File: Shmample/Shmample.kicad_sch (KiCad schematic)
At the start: 148 parts, among them J1 Conn_01x04_Socket, J2 PowerOut, Q1 BC547, Q10 BC547, Q2 BC557, Q3 BC547, Q4 BC547, Q5 BC557, Q6 BC557, Q7 BC547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

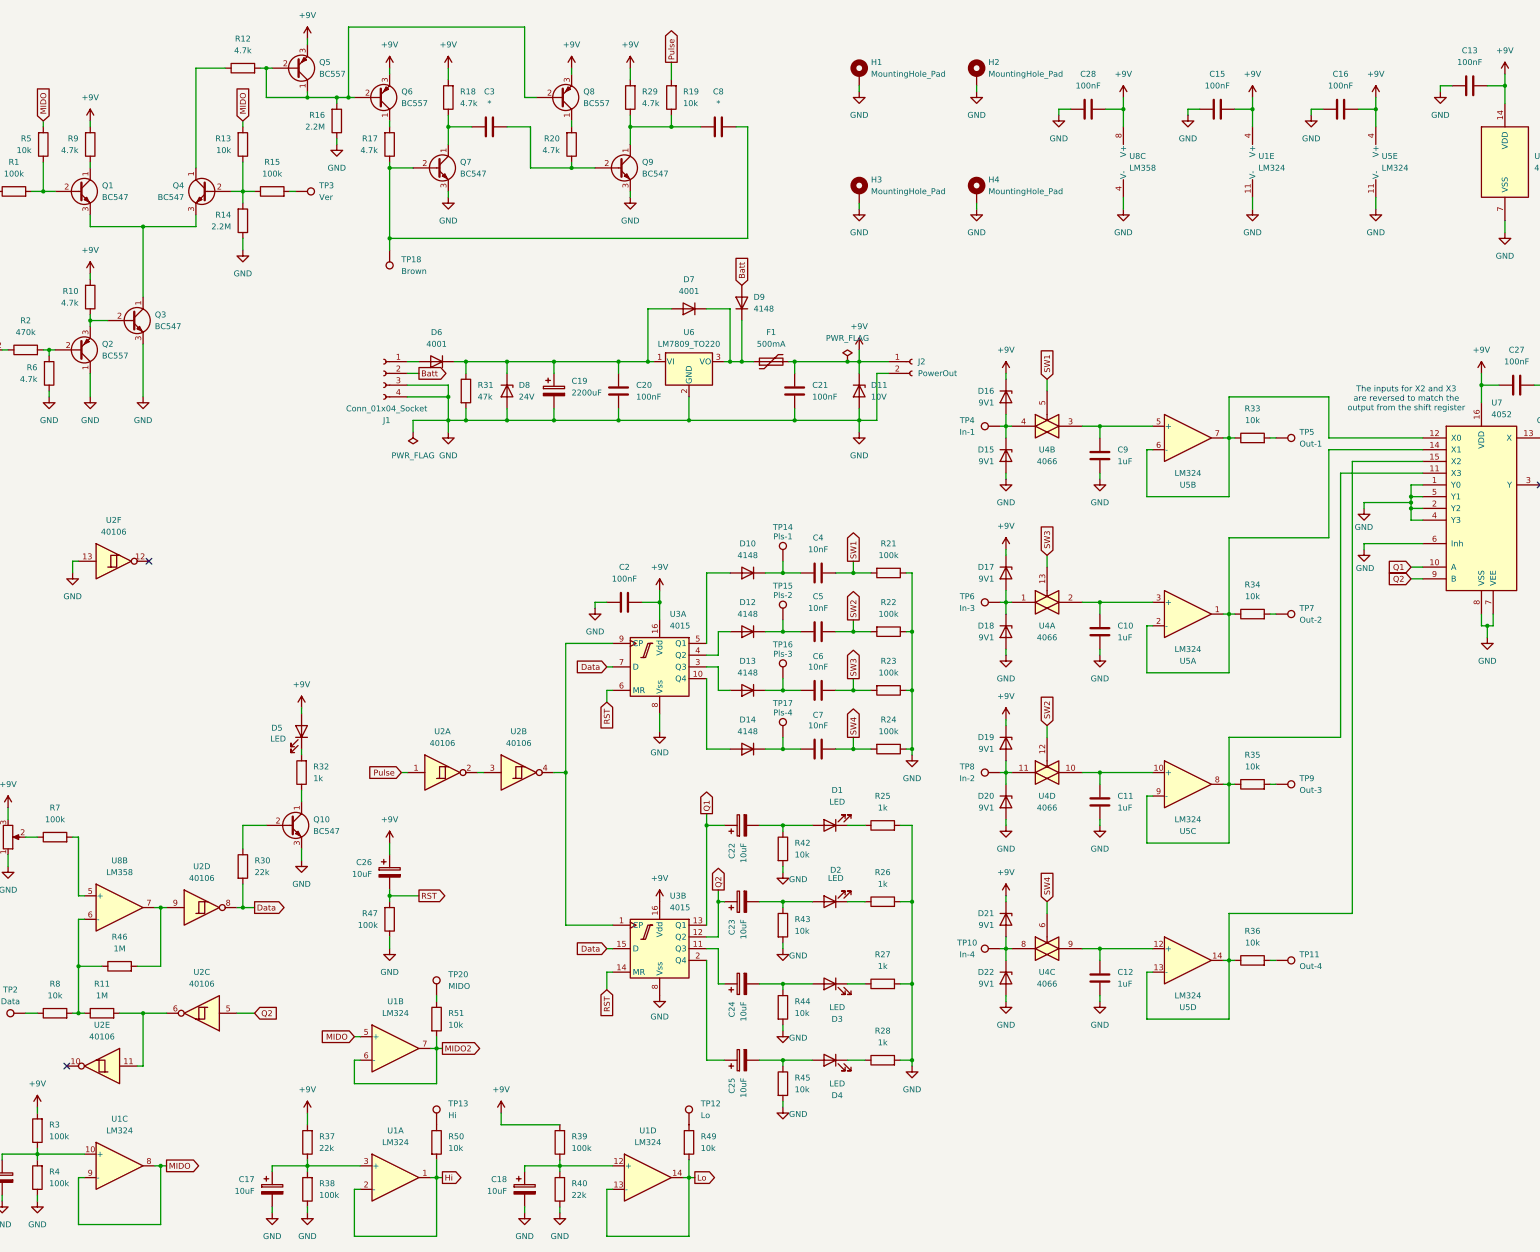
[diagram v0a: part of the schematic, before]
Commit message: Added attenuators
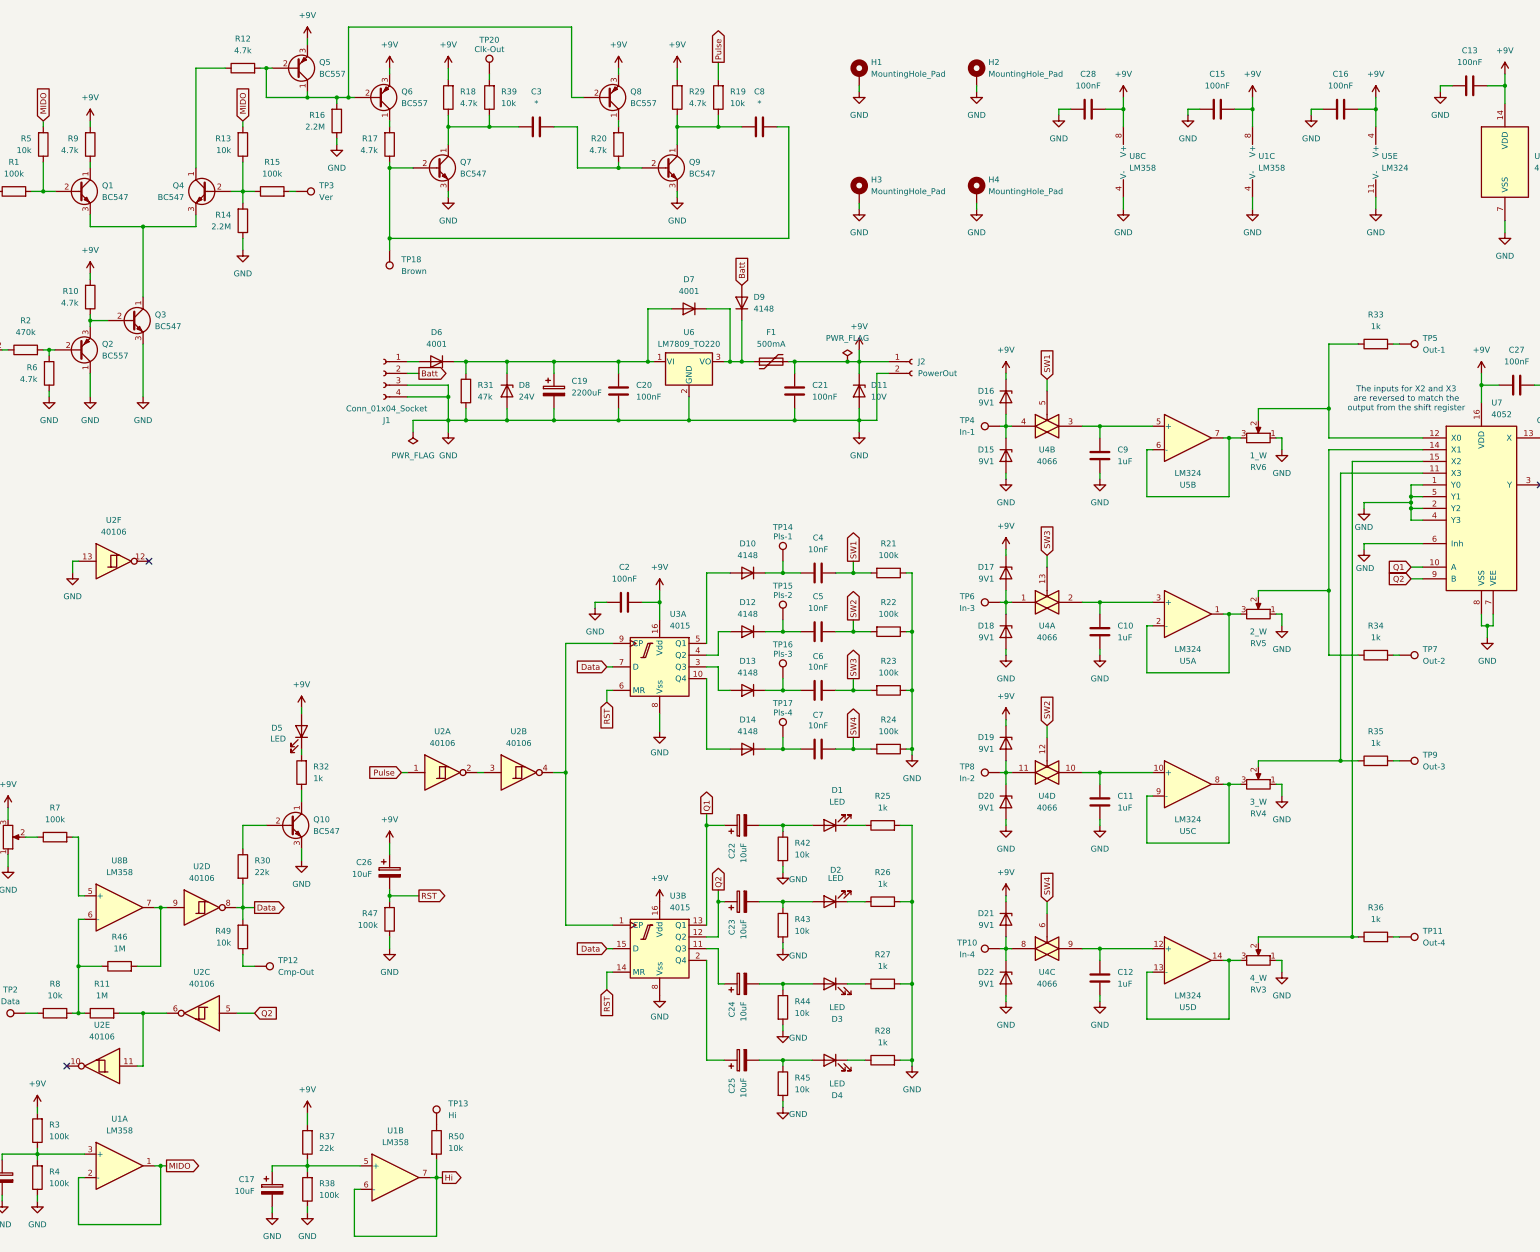
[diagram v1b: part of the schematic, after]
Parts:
- removed C18: 10uF, diy-nabra:cel1, symbol Device:C_Polarized
- removed R40: 22k, diy-nabra:r3, symbol Device:R
- removed R51: 10k, diy-nabra:r3, symbol Device:R
- removed U1: LM324, diy-nabra:dip14, symbol Amplifier_Operational:LM324
- added RV3: 4_W, diy-nabra:wnob4, symbol Device:R_Potentiometer
- added RV4: 3_W, diy-nabra:wnob3, symbol Device:R_Potentiometer
- added RV5: 2_W, diy-nabra:wnob2, symbol Device:R_Potentiometer
- added RV6: 1_W, diy-nabra:wnob1, symbol Device:R_Potentiometer
- added U1: LM358, diy-nabra:dip8, symbol Amplifier_Operational:LM358
- R33, R34, R35, R36: value 10k -> 1k
- R39: value 100k -> 10k
- TP1: footprint diy-nabra:wtrin -> diy-nabra:wtrin2
- TP12: value Lo -> Cmp-Out; footprint diy-nabra:wsqu2in -> diy-nabra:wvout
- TP13: footprint diy-nabra:wsqout -> diy-nabra:wvout
- TP20: value MIDO -> Clk-Out; footprint diy-nabra:wsqout -> diy-nabra:wclk_out
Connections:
- net Lo is gone; now on net Data: R49.2
- net +9V: now also U1.8 (V+); no longer R39.2
- net GND: now also RV3.1, RV4.1, RV5.1, RV6.1, U1.4 (V-)
- net Hi: now also U1.6 (-), U1.7
- net MIDO: now also U1.1, U1.2 (-)
- net at C17.1, R37.1, R38.2: now also U1.5 (+)
- net at R39.1: now also C3.1, Q7.1 (C), R18.1
- net at C1.1, R3.1, R4.2: now also U1.3 (+)
- net at R35.1, U7.11 (X3): now also RV4.2; no longer U5.8, U5.9 (-)
- net at TP20.1: now also R39.2
- net at R34.1, U7.14 (X1): now also RV5.2; no longer U5.1, U5.2 (-)
- net at U5.6 (-), U5.7: now also RV6.3; no longer R33.1, U7.12 (X0)
- net at R36.1, U7.15 (X2): now also RV3.2; no longer U5.13 (-), U5.14
- new net: RV4.3, U5.8, U5.9 (-)
- new net: R33.1, RV6.2, U7.12 (X0)
- new net: RV5.3, U5.1, U5.2 (-)
- new net: RV3.3, U5.13 (-), U5.14
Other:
- moved on the sheet: C3, C8, Q8, Q9, R19, R20, R29, R33, R34, R35, R36, TP11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

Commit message: Revision 1
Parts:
- removed C1, C17, C22, C23, C24, C25, C26: 10uF, diy-nabra:cel1, symbol Device:C_Polarized
- removed C10, C11, C12, C9: 1uF, diy-nabra:cpoly105, symbol Device:C
- removed C13, C14, C15, C16, C2, C20, C21, C27, C28: 100nF, diy-nabra:cpoly104_small, symbol Device:C
- removed C19: 2200uF, diy-nabra:cel2, symbol Device:C_Polarized
- removed C3, C8: *, diy-nabra:chairy, symbol Device:C
- removed C4, C5, C6, C7: 10nF, diy-nabra:cpoly103, symbol Device:C
- removed D1, D2, D3, D4, D5: LED, diy-nabra:led, symbol Device:LED
- removed D10, D12, D13, D14, D9: 4148, diy-nabra:do3, symbol Diode:1N4148
- removed D11: 10V, diy-nabra:doz3, symbol Device:D_Zener
- removed D15, D16, D17, D18, D19, D20, D21, D22: 9V1, diy-nabra:doz3, symbol Device:D_Zener
- removed D6, D7: 4001, diy-nabra:do3, symbol Diode:1N4001
- removed D8: 24V, diy-nabra:doz3, symbol Device:D_Zener
- removed F1: 500mA, Fuse:Fuse_Bourns_MF-RG500, symbol Device:Polyfuse
- removed H1, H2, H3, H4: MountingHole_Pad, MountingHole:MountingHole_3.2mm_M3_ISO7380_Pad, symbol Mechanical:MountingHole_Pad
- removed J1: Conn_01x04_Socket, diy-nabra:powern, symbol Connector:Conn_01x04_Socket
- removed J2: PowerOut, Connector_PinSocket_2.54mm:PinSocket_1x02_P2.54mm_Vertical, symbol Connector:Conn_01x02_Socket
- removed Q1, Q10, Q3, Q4, Q7, Q9: BC547, diy-nabra:qnpn, symbol Transistor_BJT:BC547
- removed Q2, Q5, Q6, Q8: BC557, diy-nabra:qpnp, symbol Transistor_BJT:BC557
- removed R1, R15, R21, R22, R23, R24, R3, R38, R4, R47, R7: 100k, diy-nabra:r3, symbol Device:R
- removed R10, R12, R17, R18, R20, R29, R6, R9: 4.7k, diy-nabra:r3, symbol Device:R
- removed R11, R46: 1M, diy-nabra:r3, symbol Device:R
- removed R13, R19, R39, R42, R43, R44, R45, R48, R49, R5, R50, R8: 10k, diy-nabra:r3, symbol Device:R
- removed R14, R16: 2.2M, diy-nabra:r3, symbol Device:R
- removed R2: 470k, diy-nabra:r3, symbol Device:R
- removed R25, R26, R27, R28, R32, R33, R34, R35, R36: 1k, diy-nabra:r3, symbol Device:R
- removed R30, R37: 22k, diy-nabra:r3, symbol Device:R
- removed R31: 47k, diy-nabra:r3, symbol Device:R
- removed R41: 100, diy-nabra:r3, symbol Device:R
- removed RV1, RV2: B50k, diy-nabra:wnob, symbol Device:R_Potentiometer
- removed RV3: 4_W, diy-nabra:wnob4, symbol Device:R_Potentiometer
- removed RV4: 3_W, diy-nabra:wnob3, symbol Device:R_Potentiometer
- removed RV5: 2_W, diy-nabra:wnob2, symbol Device:R_Potentiometer
- removed RV6: 1_W, diy-nabra:wnob1, symbol Device:R_Potentiometer
- removed TP1: Inv, diy-nabra:wtrin2, symbol Connector:TestPoint
- removed TP10: In-4, diy-nabra:wsqu4in, symbol Connector:TestPoint
- removed TP11: Out-4, diy-nabra:wtrin4, symbol Connector:TestPoint
- removed TP12: Cmp-Out, diy-nabra:wvout, symbol Connector:TestPoint
- removed TP13: Hi, diy-nabra:wvout, symbol Connector:TestPoint
- removed TP14: Pls-1, diy-nabra:wcircin, symbol Connector:TestPoint
- removed TP15: Pls-2, diy-nabra:wcirc2in, symbol Connector:TestPoint
- removed TP16: Pls-3, diy-nabra:wcirc3in, symbol Connector:TestPoint
- removed TP17: Pls-4, diy-nabra:wcirc4in, symbol Connector:TestPoint
- removed TP18: Brown, diy-nabra:wsquin, symbol Connector:TestPoint
- removed TP19: All-Out, diy-nabra:wsqout, symbol Connector:TestPoint
- removed TP2: Data, diy-nabra:wtrin, symbol Connector:TestPoint
- removed TP20: Clk-Out, diy-nabra:wclk_out, symbol Connector:TestPoint
- removed TP3: Ver, diy-nabra:wtrin, symbol Connector:TestPoint
- removed TP4: In-1, diy-nabra:wsquin, symbol Connector:TestPoint
- removed TP5: Out-1, diy-nabra:wtrin, symbol Connector:TestPoint
- removed TP6: In-3, diy-nabra:wsqu2in, symbol Connector:TestPoint
- removed TP7: Out-2, diy-nabra:wtrin2, symbol Connector:TestPoint
- removed TP8: In-2, diy-nabra:wsqu3in, symbol Connector:TestPoint
- removed TP9: Out-3, diy-nabra:wtrin3, symbol Connector:TestPoint
- removed U1, U8: LM358, diy-nabra:dip8, symbol Amplifier_Operational:LM358
- removed U2: 40106, diy-nabra:dip14, symbol 4xxx:40106
- removed U3: 4015, diy-nabra:dip16, symbol 4xxx_IEEE:4015
- removed U4: 4066, diy-nabra:dip14, symbol 4xxx:4066
- removed U5: LM324, diy-nabra:dip14, symbol Amplifier_Operational:LM324
- removed U6: LM7809_TO220, Package_TO_SOT_THT:TO-220-3_Horizontal_TabDown, symbol Regulator_Linear:LM7809_TO220
- removed U7: 4052, diy-nabra:dip16, symbol 4xxx:4052
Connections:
- no-connect marks 3 -> 0
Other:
- added sheet 2Roll (2roll.kicad_sch)
- added sheet S&H (sandh.kicad_sch)
- added sheet power (power.kicad_sch)
- added sheet shift_reg (shift_reg.kicad_sch)
- note removed: "The inputs for X2 and X3 are reversed to match the output from the shift register"
